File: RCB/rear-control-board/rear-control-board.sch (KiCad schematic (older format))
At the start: 5 parts

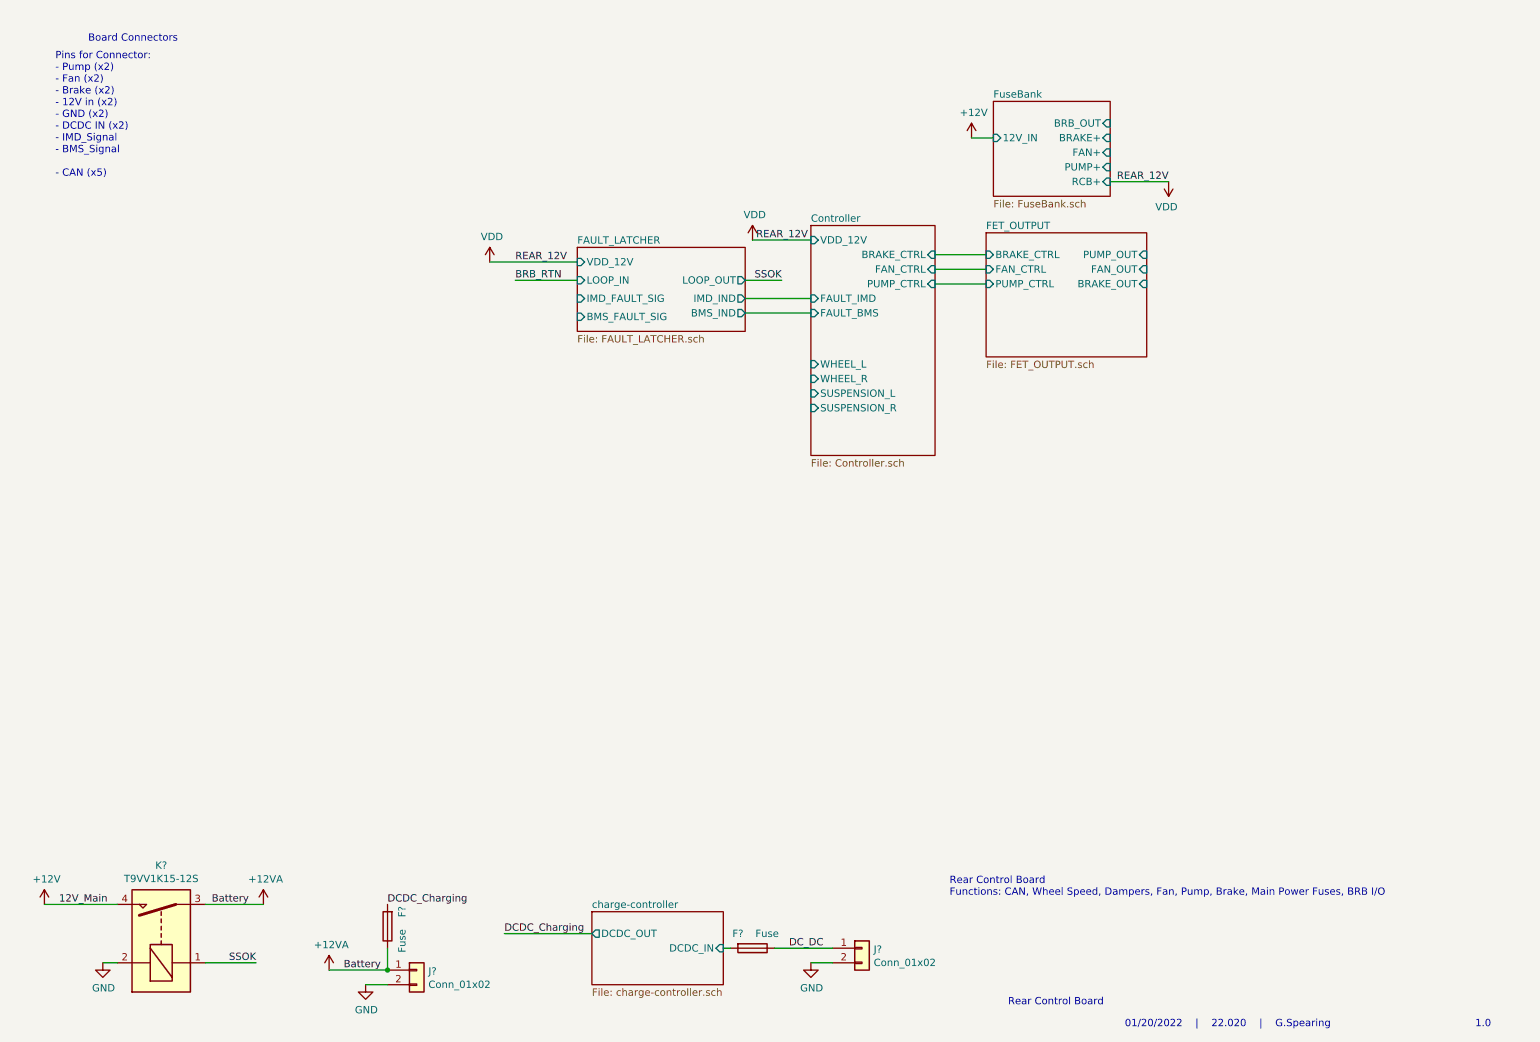
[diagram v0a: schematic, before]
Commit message: finish schematic, start layout
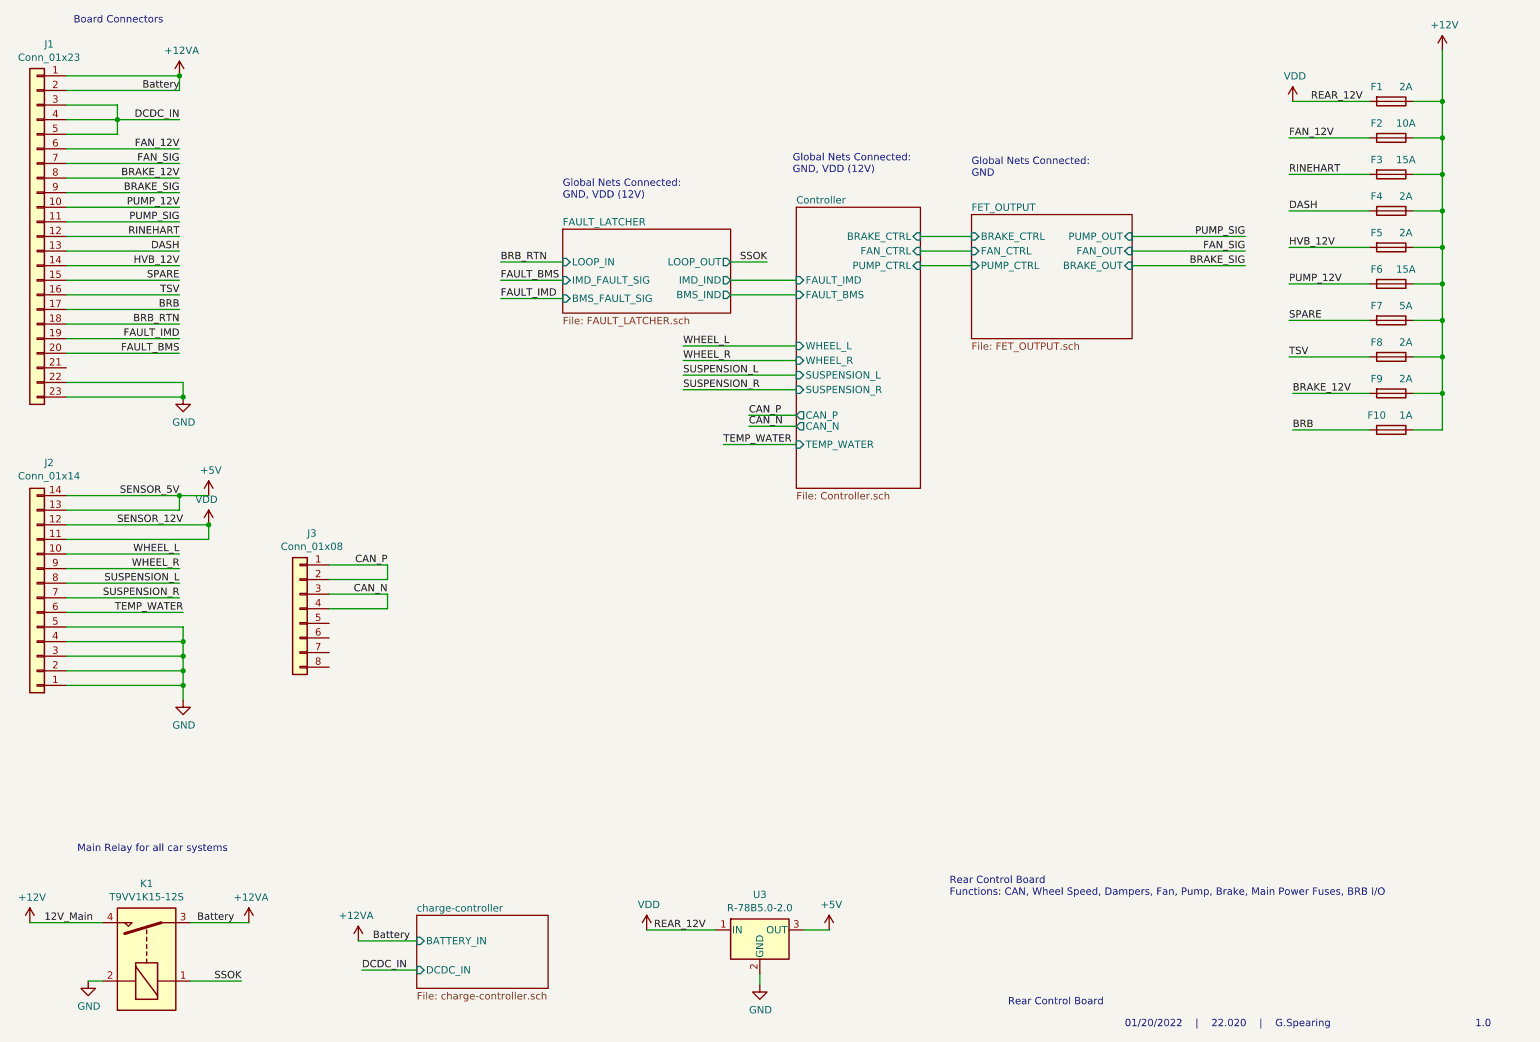
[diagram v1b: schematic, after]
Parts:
- removed F? (x2): Fuse, symbol Device:Fuse
- removed J? (x2): Conn_01x02, symbol Connector_Generic:Conn_01x02
- added F1, F4, F5, F8, F9: 2A, AERO_Footprints:Fuseholder_Blade_Mini_Keystone_3568, symbol Device:Fuse
- added F10: 1A, AERO_Footprints:Fuseholder_Blade_Mini_Keystone_3568, symbol Device:Fuse
- added F2: 10A, AERO_Footprints:Fuseholder_Blade_Mini_Keystone_3568, symbol Device:Fuse
- added F3, F6: 15A, AERO_Footprints:Fuseholder_Blade_Mini_Keystone_3568, symbol Device:Fuse
- added F7: 5A, AERO_Footprints:Fuseholder_Blade_Mini_Keystone_3568, symbol Device:Fuse
- added J1: Conn_01x23, AERO_Footprints:TE_1-770669-1_23pin_Horizontal, symbol Connector_Generic:Conn_01x23
- added J2: Conn_01x14, AERO_Footprints:TE_1-776266-1_14pin_Horizontal, symbol Connector_Generic:Conn_01x14
- added J3: Conn_01x08, AERO_Footprints:TE_1-776280-1_8pin_Horizontal, symbol Connector_Generic:Conn_01x08
- added U3: R-78B5.0-2.0, Converter_DCDC:Converter_DCDC_RECOM_R-78B-2.0_THT, symbol Regulator_Switching:R-78B5.0-2.0
- K1: renamed from K?; footprint AERO-footprints:RELAY_T9VV1K15-12S -> AERO_Footprints:RELAY_T9VV1K15-12S
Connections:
- net +12V: now also F1.1, F10.1, F2.1, F3.1, F4.1, F5.1, F6.1, F7.1, F8.1, F9.1
- net +12VA: now also J1.1 (Pin_1), J1.2 (Pin_2)
- net BRB_RTN: now also J1.18 (Pin_18)
- net GND: now also J1.22 (Pin_22), J1.23 (Pin_23), J2.1 (Pin_1), J2.2 (Pin_2), J2.3 (Pin_3), J2.4 (Pin_4), J2.5 (Pin_5), U3.2 (GND)
- net VDD: now also F1.2, J2.11 (Pin_11), J2.12 (Pin_12), U3.1 (IN)
- new net +5V: J2.13 (Pin_13), J2.14 (Pin_14), U3.3 (OUT)
- new net BRAKE_12V: F9.2, J1.8 (Pin_8)
- new net BRAKE_SIG: J1.9 (Pin_9)
- new net BRB: F10.2, J1.17 (Pin_17)
- new net CAN_N: J3.3 (Pin_3), J3.4 (Pin_4)
- new net CAN_P: J3.1 (Pin_1), J3.2 (Pin_2)
- new net DASH: F4.2, J1.13 (Pin_13)
- new net DCDC_IN: J1.3 (Pin_3), J1.4 (Pin_4), J1.5 (Pin_5)
- new net FAN_12V: F2.2, J1.6 (Pin_6)
- new net FAN_SIG: J1.7 (Pin_7)
- new net FAULT_BMS: J1.20 (Pin_20)
- new net FAULT_IMD: J1.19 (Pin_19)
- new net HVB_12V: F5.2, J1.14 (Pin_14)
- new net PUMP_12V: F6.2, J1.10 (Pin_10)
- new net PUMP_SIG: J1.11 (Pin_11)
- new net RINEHART: F3.2, J1.12 (Pin_12)
- new net SPARE: F7.2, J1.15 (Pin_15)
- new net SUSPENSION_L: J2.8 (Pin_8)
- new net SUSPENSION_R: J2.7 (Pin_7)
- new net TEMP_WATER: J2.6 (Pin_6)
- new net TSV: F8.2, J1.16 (Pin_16)
- new net WHEEL_L: J2.10 (Pin_10)
- new net WHEEL_R: J2.9 (Pin_9)
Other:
- note added: "Global Nets Connected: \nGND"
- note added: "Global Nets Connected: \nGND, VDD (12V)"
- note added: "Main Relay for all car systems"
- note removed: "Pins for Connector: \n- Pump (x2)\n- Fan (x2)\n- Brake (x2)\n- 12V in (x2)\n- GND (x2)\n- DCDC IN (x2)\n- IMD_Signal\n- BMS_Signal\n\n- CAN (x5)"
- moved on the sheet: K1

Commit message: working on layout
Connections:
- net +12V: no longer F8.1
- net SSOK: now also F8.1
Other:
- moved on the sheet: F8
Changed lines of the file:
@@
 L Device:Fuse F8
 U 1 1 6219EA74
-P 10025 3050
-F 0 "F8" V 9925 2950 50  0000 C CNN
-F 1 "2A" V 9925 3150 50  0000 C CNN
-F 2 "AERO_Footprints:Fuseholder_Blade_Mini_Keystone_3568" V 9955 3050 50  0001 C CNN
-F 3 "~" H 10025 3050 50  0001 C CNN
-	1    10025 3050
+P 9900 4000
+F 0 "F8" V 9800 3900 50  0000 C CNN
+F 1 "2A" V 9800 4100 50  0000 C CNN
+F 2 "AERO_Footprints:Fuseholder_Blade_Mini_Keystone_3568" V 9830 4000 50  0001 C CNN
+F 3 "~" H 9900 4000 50  0001 C CNN
+	1    9900 4000
 	0    1    1    0
 $EndComp
@@
 Text Label 9325 2800 0    50   ~ 0
 SPARE
-Text Label 9325 3050 0    50   ~ 0
+Text Label 9325 4000 0    50   ~ 0
 TSV
 $Comp
@@
 	9325 2800 9875 2800
 Wire Wire Line
-	9325 3050 9875 3050
+	9325 4000 9750 4000
 Wire Wire Line
 	10375 3550 10175 3550
@@
 	10375 3300 10375 3550
 Wire Wire Line
-	10175 3050 10375 3050
-Connection ~ 10375 3050
-Wire Wire Line
-	10375 3050 10375 3300
+	10050 4000 10375 4000
 Wire Wire Line
 	10175 2800 10375 2800
 Connection ~ 10375 2800
-Wire Wire Line
-	10375 2800 10375 3050
 Wire Wire Line
 	10175 2550 10375 2550
@@
 	-1   0    0    -1
 $EndComp
+Wire Wire Line
+	10375 2800 10375 3300
+Text Label 10375 4000 2    50   ~ 0
+SSOK
 $EndSCHEMATC

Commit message: layout and connector pins
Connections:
- net +12VA: now also J1.11 (Pin_11), J1.12 (Pin_12), J1.5 (Pin_5); no longer J1.1 (Pin_1), J1.2 (Pin_2)
- net BRAKE_12V: now also J1.4 (Pin_4); no longer J1.8 (Pin_8)
- net BRAKE_SIG: now also J1.7 (Pin_7); no longer J1.9 (Pin_9)
- net BRB: now also J1.18 (Pin_18); no longer J1.17 (Pin_17)
- net BRB_RTN: now also J1.19 (Pin_19); no longer J1.18 (Pin_18)
- net CAN_N: now also J3.2 (Pin_2); no longer J3.3 (Pin_3)
- net CAN_P: now also J3.3 (Pin_3), J3.5 (Pin_5); no longer J3.1 (Pin_1), J3.2 (Pin_2)
- net DASH: now also J1.16 (Pin_16); no longer J1.13 (Pin_13)
- net DCDC_IN: now also J1.13 (Pin_13), J1.14 (Pin_14), J1.6 (Pin_6); no longer J1.3 (Pin_3), J1.4 (Pin_4), J1.5 (Pin_5)
- net FAN_12V: now also J1.2 (Pin_2); no longer J1.6 (Pin_6)
- net FAN_SIG: now also J1.8 (Pin_8); no longer J1.7 (Pin_7)
- net FAULT_BMS: now also J1.22 (Pin_22); no longer J1.20 (Pin_20)
- net FAULT_IMD: now also J1.10 (Pin_10); no longer J1.19 (Pin_19)
- net GND: now also J1.20 (Pin_20), J1.21 (Pin_21); no longer J1.22 (Pin_22), J1.23 (Pin_23)
- net HVB_12V: now also J1.17 (Pin_17); no longer J1.14 (Pin_14)
- net PUMP_12V: now also J1.9 (Pin_9); no longer J1.10 (Pin_10)
- net PUMP_SIG: now also J1.15 (Pin_15); no longer J1.11 (Pin_11)
- net RINEHART: now also J1.1 (Pin_1); no longer J1.12 (Pin_12)
- net SPARE: now also J1.3 (Pin_3); no longer J1.15 (Pin_15)
- net TSV: now also J1.23 (Pin_23); no longer J1.16 (Pin_16)
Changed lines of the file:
@@
 	-1   0    0    -1
 $EndComp
-Text Label 1725 2025 2    50   ~ 0
+Text Label 1725 1925 2    50   ~ 0
 PUMP_12V
 Wire Wire Line
-	1725 2025 950  2025
-Text Label 1725 2125 2    50   ~ 0
+	1725 1925 950  1925
+Text Label 1725 2525 2    50   ~ 0
 PUMP_SIG
 Wire Wire Line
-	1725 2125 950  2125
-Text Label 1725 1625 2    50   ~ 0
+	1725 2525 950  2525
+Text Label 1725 1225 2    50   ~ 0
 FAN_12V
 Wire Wire Line
-	1725 1625 950  1625
+	1725 1225 950  1225
+Text Label 1725 1825 2    50   ~ 0
+FAN_SIG
+Wire Wire Line
+	1725 1825 950  1825
+Text Label 1725 1425 2    50   ~ 0
+BRAKE_12V
+Wire Wire Line
+	1725 1425 950  1425
 Text Label 1725 1725 2    50   ~ 0
-FAN_SIG
+BRAKE_SIG
 Wire Wire Line
 	1725 1725 950  1725
-Text Label 1725 1825 2    50   ~ 0
-BRAKE_12V
-Wire Wire Line
-	1725 1825 950  1825
-Text Label 1725 1925 2    50   ~ 0
-BRAKE_SIG
-Wire Wire Line
-	1725 1925 950  1925
 $Sheet
 S 7150 2075 1100 850
@@
 Wire Wire Line
 	6800 2425 7150 2425
-$Comp
-L power:+12VA #PWR0107
-U 1 1 6217930C
-P 1725 1125
-F 0 "#PWR0107" H 1725 975 50  0001 C CNN
-F 1 "+12VA" H 1740 1298 50  0000 C CNN
-F 2 "" H 1725 1125 50  0001 C CNN
-F 3 "" H 1725 1125 50  0001 C CNN
-	1    1725 1125
-	1    0    0    -1
-$EndComp
-Wire Wire Line
-	1725 1125 950  1125
-Wire Wire Line
-	950  1225 1725 1225
-Wire Wire Line
-	1725 1225 1725 1125
-Connection ~ 1725 1125
-Text Label 1725 1425 2    50   ~ 0
+Text Label 1700 2325 2    50   ~ 0
 DCDC_IN
-Text Label 1725 1225 2    50   ~ 0
-Battery
-Wire Wire Line
-	950  1425 1300 1425
-Wire Wire Line
-	950  1325 1300 1325
-Wire Wire Line
-	1300 1325 1300 1425
-Connection ~ 1300 1425
-Wire Wire Line
-	1300 1425 1725 1425
 $Comp
 L power:GND #PWR0108
 U 1 1 6218B3DC
-P 1750 3325
-F 0 "#PWR0108" H 1750 3075 50  0001 C CNN
-F 1 "GND" H 1755 3152 50  0000 C CNN
-F 2 "" H 1750 3325 50  0001 C CNN
-F 3 "" H 1750 3325 50  0001 C CNN
-	1    1750 3325
-	1    0    0    -1
-$EndComp
-Wire Wire Line
-	1750 3325 950  3325
+P 2025 3025
+F 0 "#PWR0108" H 2025 2775 50  0001 C CNN
+F 1 "GND" H 2030 2852 50  0000 C CNN
+F 2 "" H 2025 3025 50  0001 C CNN
+F 3 "" H 2025 3025 50  0001 C CNN
+	1    2025 3025
+	1    0    0    -1
+$EndComp
 Wire Wire Line
 	950  5300 1750 5300
 Wire Wire Line
 	1750 5300 1750 5400
-Connection ~ 1750 3325
-Wire Wire Line
-	950  3225 1750 3225
-Wire Wire Line
-	1750 3225 1750 3325
 $Comp
 L Device:Fuse F1
@@
 	1    0    0    -1
 $EndComp
-Text Label 1725 2225 2    50   ~ 0
+Text Label 1725 1125 2    50   ~ 0
 RINEHART
 Wire Wire Line
-	1725 2225 950  2225
-Text Label 1725 2325 2    50   ~ 0
+	1725 1125 950  1125
+Text Label 1725 2625 2    50   ~ 0
 DASH
-Wire Wire Line
-	1725 2325 950  2325
-Text Label 1725 2425 2    50   ~ 0
-HVB_12V
-Wire Wire Line
-	1725 2425 950  2425
-Text Label 1725 2525 2    50   ~ 0
-SPARE
-Wire Wire Line
-	1725 2525 950  2525
-Text Label 1725 2625 2    50   ~ 0
-TSV
 Wire Wire Line
 	1725 2625 950  2625
 Text Label 1725 2725 2    50   ~ 0
+HVB_12V
+Wire Wire Line
+	1725 2725 950  2725
+Text Label 1725 1325 2    50   ~ 0
+SPARE
+Wire Wire Line
+	1725 1325 950  1325
+Text Label 1725 3325 2    50   ~ 0
+TSV
+Wire Wire Line
+	1725 3325 950  3325
+Text Label 1725 2825 2    50   ~ 0
 BRB
-Wire Wire Line
-	1725 2725 950  2725
-Text Label 1725 2825 2    50   ~ 0
+Text Label 1725 2925 2    50   ~ 0
 BRB_RTN
 Wire Wire Line
-	1725 2825 950  2825
+	1725 2925 950  2925
 $Comp
 L power:VDD #PWR0110
@@
 Text Notes 1025 6450 0    50   ~ 0
 Main Relay for all car systems
-Text Label 3150 4475 2    50   ~ 0
+Text Label 3150 4875 2    50   ~ 0
 CAN_P
 Text Label 5625 3450 0    50   ~ 0
@@
 Wire Wire Line
 	5175 2975 5950 2975
-Text Label 3150 4675 2    50   ~ 0
+Text Label 3150 4575 2    50   ~ 0
 CAN_N
 Wire Wire Line
-	3150 4475 2750 4475
-Wire Wire Line
-	3150 4675 2750 4675
+	3150 4875 2750 4875
+Wire Wire Line
+	3150 4575 2750 4575
 Text Label 5625 3525 0    50   ~ 0
 CAN_N
 Wire Wire Line
 	5625 3525 5950 3525
-Wire Wire Line
-	2750 4575 3150 4575
-Wire Wire Line
-	3150 4575 3150 4475
-Wire Wire Line
-	2750 4775 3150 4775
-Wire Wire Line
-	3150 4775 3150 4675
 $Comp
 L Regulator_Switching:R-78B5.0-2.0 U3
@@
 Wire Wire Line
 	1750 5000 1750 5100
-Wire Wire Line
-	950  1525 1300 1525
-Wire Wire Line
-	1300 1525 1300 1425
-Text Label 1725 2925 2    50   ~ 0
+Text Label 1725 2025 2    50   ~ 0
 FAULT_IMD
 Wire Wire Line
-	1725 2925 950  2925
-Text Label 1725 3025 2    50   ~ 0
+	1725 2025 950  2025
+Text Label 1725 3225 2    50   ~ 0
 FAULT_BMS
 Wire Wire Line
-	1725 3025 950  3025
+	1725 3225 950  3225
 Text Label 3925 2650 0    50   ~ 0
 FAULT_IMD
@@
 Text Label 10375 4000 2    50   ~ 0
 SSOK
+Wire Wire Line
+	1700 2325 1375 2325
+Wire Wire Line
+	950  2425 1375 2425
+Wire Wire Line
+	1375 2425 1375 2325
+Connection ~ 1375 2325
+Wire Wire Line
+	1375 2325 950  2325
+Text Label 1725 1625 2    50   ~ 0
+DCDC_IN
+Wire Wire Line
+	1725 1625 950  1625
+Text Label 1725 1525 2    50   ~ 0
+Battery
+Text Label 1725 2225 2    50   ~ 0
+Battery
+$Comp
+L power:+12VA #PWR0107
+U 1 1 61F1F158
+P 1850 2225
+F 0 "#PWR0107" H 1850 2075 50  0001 C CNN
+F 1 "+12VA" H 1865 2398 50  0000 C CNN
+F 2 "" H 1850 2225 50  0001 C CNN
+F 3 "" H 1850 2225 50  0001 C CNN
+	1    1850 2225
+	1    0    0    -1
+$EndComp
+Wire Wire Line
+	950  2225 1375 2225
+Wire Wire Line
+	950  1525 1850 1525
+$Comp
+L power:+12VA #PWR0138
+U 1 1 61F18DE9
+P 1850 1525
+F 0 "#PWR0138" H 1850 1375 50  0001 C CNN
+F 1 "+12VA" H 1865 1698 50  0000 C CNN
+F 2 "" H 1850 1525 50  0001 C CNN
+F 3 "" H 1850 1525 50  0001 C CNN
+	1    1850 1525
+	1    0    0    -1
+$EndComp
+Wire Wire Line
+	950  2125 1375 2125
+Wire Wire Line
+	1375 2125 1375 2225
+Connection ~ 1375 2225
+Wire Wire Line
+	1375 2225 1850 2225
+Wire Wire Line
+	950  2825 1725 2825
+Text Label 3150 4675 2    50   ~ 0
+CAN_P
+Wire Wire Line
+	3150 4675 2750 4675
+Text Label 3150 4775 2    50   ~ 0
+CAN_N
+Wire Wire Line
+	3150 4775 2750 4775
+Wire Wire Line
+	950  3025 1725 3025
+Wire Wire Line
+	950  3125 1725 3125
+Wire Wire Line
+	1725 3125 1725 3025
+Connection ~ 1725 3025
+Wire Wire Line
+	1725 3025 2025 3025
 $EndSCHEMATC
